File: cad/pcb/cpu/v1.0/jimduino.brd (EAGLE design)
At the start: 38 x 31 mm, 59 parts, among them CN1 SM02B-SRSS-TB, P1 DF12-32-DP, P2 DF12-32-DP, P3 MICROUSB, Q1 FDN360P, Q2 FDN360P, SW1 SWITCH-MOMENTARY-2SMD-REDUNDA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, U1 STM32F415R, U2 MCP1703, U3 MCP73831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

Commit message: Release candidate 0
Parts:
- C7, C8: value 20pF -> 22pF
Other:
- board text removed: "BKUP"
- board text removed: "BOOT0"
- board text removed: "C1"
- board text removed: "C10"
- board text removed: "C11"
- board text removed: "C12"
- board text removed: "C13"
- board text removed: "C14"
- board text removed: "C15"
- board text removed: "C16"
- board text removed: "C17"
- board text removed: "C18"
- board text removed: "C19"
- board text removed: "C2"
- board text removed: "C20"
- board text removed: "C21"
- board text removed: "C3"
- board text removed: "C4"
- board text removed: "C5"
- board text removed: "C6"
- board text removed: "C7"
- board text removed: "C8"
- board text removed: "C9"
- board text removed: "CN1"
- board text removed: "D1"
- board text removed: "D2"
- board text removed: "D3"
- board text removed: "D5"
- board text removed: "F1"
- board text removed: "P1"
- board text removed: "P2"
- board text removed: "POWER"
- board text removed: "Q1"
- board text removed: "Q2"
- board text removed: "R1"
- board text removed: "R10"
- board text removed: "R11"
- board text removed: "R12"
- board text removed: "R2"
- board text removed: "R3"
- board text removed: "R4"
- board text removed: "R5"
- board text removed: "R6"
- board text removed: "R7"
- board text removed: "R8"
- board text removed: "R9"
- board text removed: "RESET"
- board text removed: "SW1"
- board text removed: "U1"
- board text removed: "U2"
- board text removed: "U3"
- board text removed: "U4"
- board text removed: "Y1"

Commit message: Release Candidate 1
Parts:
- C7, C8: value 22pF -> 20pF
- moved C1 0.12 mm to (23.5, 2.75)
- moved C4 0.12 mm to (21.8, 2.75)
- moved C7 0.12 mm to (15.5, 2.75), turned to 90 degrees
- moved C8 0.12 mm to (20.0, 2.75)
- turned R5 to 270 degrees
- turned Y1 to 180 degrees
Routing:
- net PC13: track 35.6 -> 33.1 mm
- net OSC_OUT: track 7.42 -> 5.06 mm
- net GND: track 2.16 -> 0.45 mm, vias 19 -> 17
- net OSC_IN: track 4.88 -> 6.32 mm
- net RESET#: track 74.4 -> 73.3 mm
- net PA2: track 17.0 -> 17.8 mm

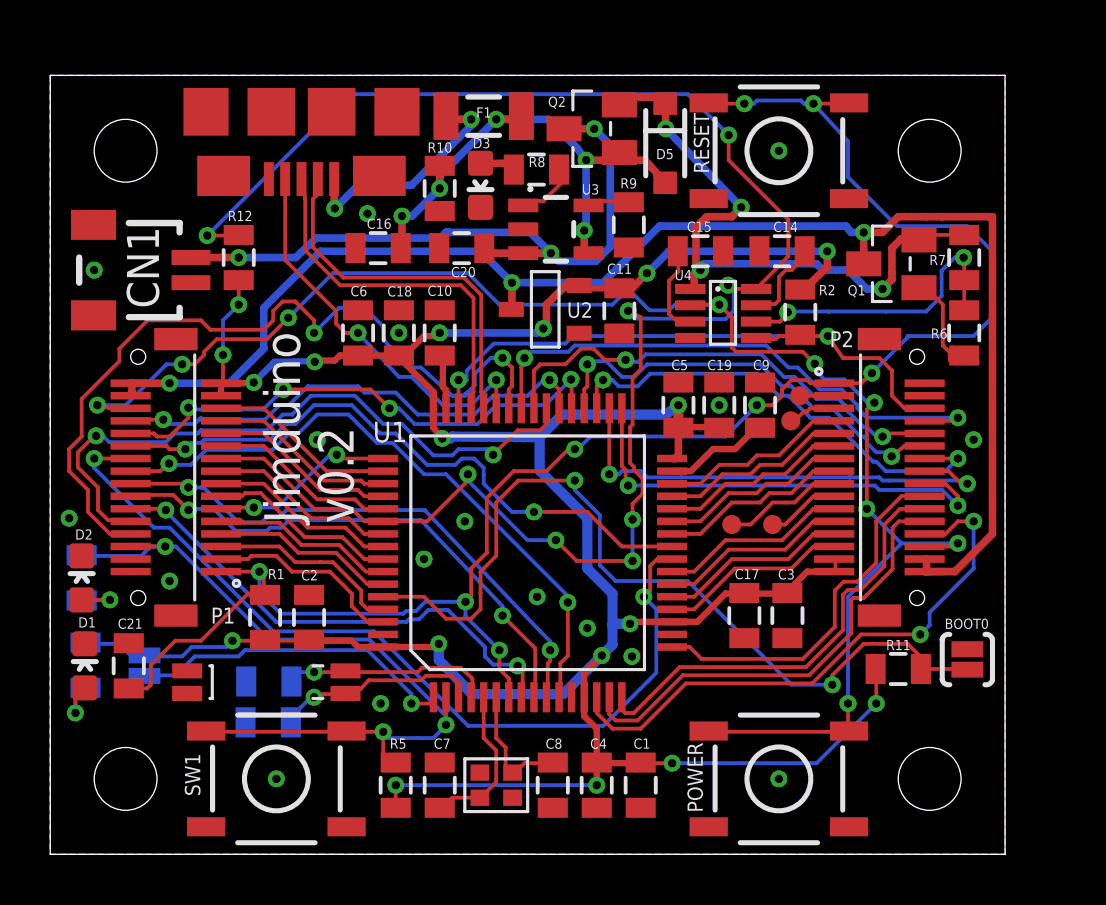
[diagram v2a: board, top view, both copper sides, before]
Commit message: Switch to 0402 capacitors
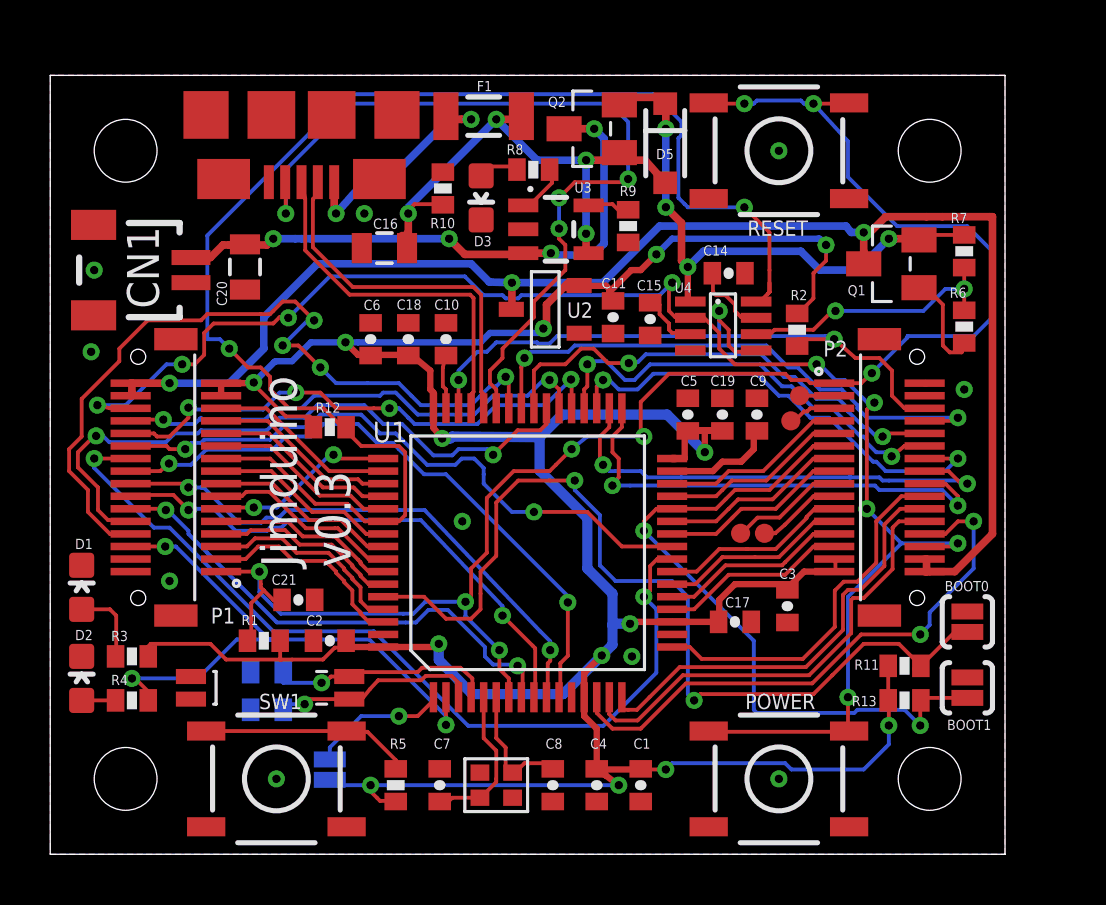
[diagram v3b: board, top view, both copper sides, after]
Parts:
- added BOOT1: JUMPER-PAD-2-NC_BY_PASTE, SparkFun-Passives:PAD-JUMPER-2-NC_BY_PASTE_YES_SILK
- added R13: 10k, SparkFun-Passives:0402-RES
- C1, C10, C11, C12, C13, C14, C15, C17, C18, C19, C2, C21, C3, C4, C5, C6, C7, C8, C9: device SparkFun-Capacitors:0805 -> SparkFun-Capacitors:0402-CAP
- R1, R10, R11, R12, R2, R3, R4, R5, R6, R7, R8, R9: device SparkFun-Passives:0805 -> SparkFun-Passives:0402-RES
- moved C20 8.66 mm to (7.75, 23.4), turned to 270 degrees
- moved BKUP 8.45 mm to (11.1, 3.38), turned to 270 degrees
- moved R12 7.66 mm to (11.1, 17.0), turned to 0 degrees
- moved C21 7.24 mm to (9.88, 10.1), turned to 0 degrees
- moved R4 5.27 mm to (3.25, 6.12), flipped to the top, turned to 0 degrees
- moved D2 4.00 mm to (1.25, 7.00)
- moved C15 3.36 mm to (23.9, 21.3), turned to 270 degrees
- moved D1 3.13 mm to (1.25, 10.6)
- moved C14 2.30 mm to (27.0, 23.1), turned to 0 degrees
- moved R3 1.88 mm to (3.25, 7.88), flipped to the top, turned to 0 degrees
- moved BOOT0 1.50 mm to (36.5, 9.25)
- moved C2 1.24 mm to (11.1, 8.50), turned to 180 degrees
- moved R1 0.93 mm to (8.50, 8.50), turned to 0 degrees
- moved R2 0.71 mm to (29.7, 20.9)
- moved C6 0.56 mm to (12.8, 20.5)
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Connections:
- new net PC14: R5.1, SW1.1, SW1.2
- net GND: now also BOOT1.2
- net PB2: now also BOOT1.1, R13.1
- net PC13: no longer R5.1, SW1.1, SW1.2
- net VCC_3V3: now also R13.2
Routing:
- net PB2: track 7.49 -> 28.0 mm, vias 0 -> 2
- net PA10: track 16.0 -> 33.7 mm, vias 2 -> 4
- net VCC_3V3: track 126.1 -> 142.3 mm, vias 18 -> 14
- net PD2: track 70.4 -> 58.1 mm, vias 8 -> 2
- net PC13: track 33.1 -> 24.5 mm
- net PC14: track 0.00 -> 8.37 mm
- net VCC_BKUP: track 13.6 -> 5.50 mm
- net VBAT: track 28.5 -> 23.7 mm, vias 3 -> 4
- net RESET#: track 73.3 -> 70.0 mm
- net BOOT0: track 34.8 -> 37.8 mm
- net N$3: track 5.33 -> 2.55 mm
- net PA13: track 25.6 -> 28.0 mm, vias 2 -> 3
- net N$8: track 12.8 -> 10.7 mm
- net VCC_SEL: track 26.0 -> 23.9 mm
- net N$4: track 4.50 -> 3.06 mm
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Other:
- board text added: "Jimduino v0.3"
- board text removed: "Jimduino v0.2"

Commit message: Release Candidate 2
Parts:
- BOOT0, BOOT1: value JUMPER-PAD-2-NC_BY_PASTE -> JUMPER-PAD-2-NOYES_SILK; device SparkFun-Passives:PAD-JUMPER-2-NC_BY_PASTE_YES_SILK -> SparkFun-Passives:PAD-JUMPER-2-NO_YES_SILK
- C1, C10, C11, C14, C15, C17, C18, C19, C2, C21, C3, C4, C5, C6, C9: device SparkFun-Capacitors:0402-CAP -> SparkFun-Capacitors:0805
- C12, C13: value 20pF -> 4pF
- C7, C8: value 20pF -> 4pF; device SparkFun-Capacitors:0402-CAP -> SparkFun-Capacitors:0805
- D2: value PC13 -> BOOT1
- R1, R10, R11, R12, R13, R2, R3, R4, R5, R6, R7, R8, R9: device SparkFun-Passives:0402-RES -> SparkFun-Passives:0805
- Y1: value 8Y-16.000MAAV-T -> 16MHz(9pF)
- Y2: value 32.768kHz -> 32.768kHz (9pF)
- moved D1 24.0 mm to (23.2, 1.12), turned to 90 degrees
- moved R3 23.5 mm to (26.7, 6.53)
- moved R4 15.5 mm to (18.0, 1.23)
- moved D2 14.8 mm to (14.9, 1.12), turned to 90 degrees
- moved BKUP 8.98 mm to (3.75, 8.50), turned to 90 degrees
- moved C20 8.80 mm to (16.4, 25.1), turned to 180 degrees
- moved R12 8.56 mm to (7.50, 24.8), turned to 90 degrees
- moved C21 6.94 mm to (3.12, 8.50), turned to 90 degrees
- moved C15 4.21 mm to (25.9, 25.0), turned to 0 degrees
- moved C14 2.83 mm to (29.1, 25.0), turned to 180 degrees
- moved C2 2.09 mm to (10.3, 10.4), turned to 90 degrees
- moved R1 1.93 mm to (8.55, 10.4), turned to 270 degrees
- moved C13 1.85 mm to (7.05, 6.28), flipped to the top, turned to 180 degrees
- moved R2 1.70 mm to (29.9, 22.6)
- moved C12 1.52 mm to (10.1, 6.28), flipped to the top
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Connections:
- removed net PC14: R5.1, SW1.1, SW1.2
- net GND: now also R11.2, R13.2; no longer BOOT0.2, BOOT1.2
- net PB2: now also R4.2
- net PC13: now also R5.1, SW1.1, SW1.2; no longer R4.2
- net VCC_3V3: now also BOOT0.2, BOOT1.2; no longer R11.2, R13.2
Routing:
- net PB2: track 28.0 -> 47.0 mm, vias 2 -> 4
- net PA10: track 33.7 -> 16.0 mm, vias 4 -> 2
- net PD2: track 58.1 -> 70.9 mm, vias 2 -> 8
- net PC14: track 8.37 -> 0.00 mm
- net VCC_BKUP: track 5.50 -> 13.6 mm
- net VCC_3V3: track 142.3 -> 135.2 mm, vias 14 -> 18
- net PC13: track 24.5 -> 31.2 mm
- net VBAT: track 23.7 -> 28.5 mm, vias 4 -> 3
- net PWR_ON: track 62.7 -> 67.0 mm
- net N$5: track 3.13 -> 7.34 mm, vias 0 -> 1
- net RESET#: track 70.0 -> 73.3 mm
- net N$3: track 2.55 -> 5.33 mm
- net BOOT0: track 37.8 -> 35.2 mm
- net PA13: track 28.0 -> 25.6 mm, vias 3 -> 2
- net N$8: track 10.7 -> 12.8 mm
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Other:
- board size 38 x 31 mm -> 38 x 32 mm
- board text added: "MatchBox v1.0"
- board text removed: "Jimduino v0.3"

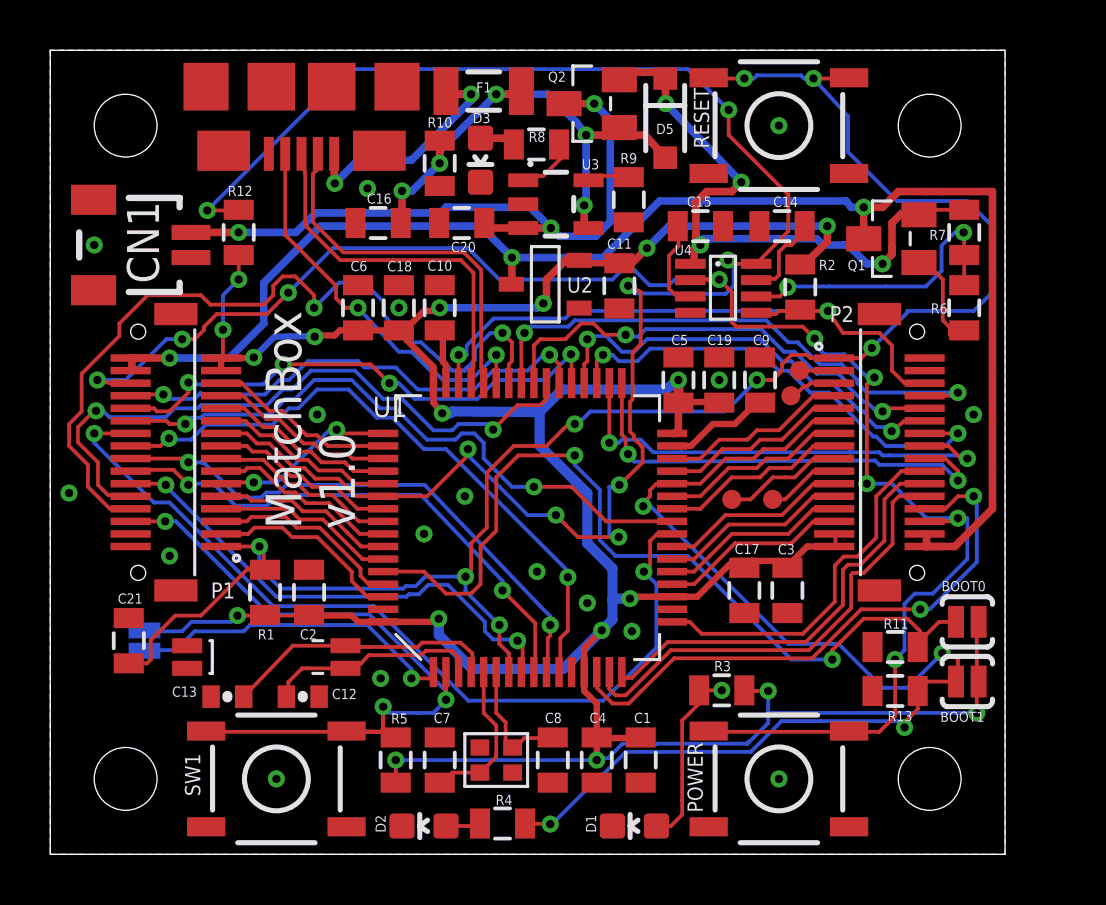
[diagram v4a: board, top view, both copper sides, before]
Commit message: New USB connector
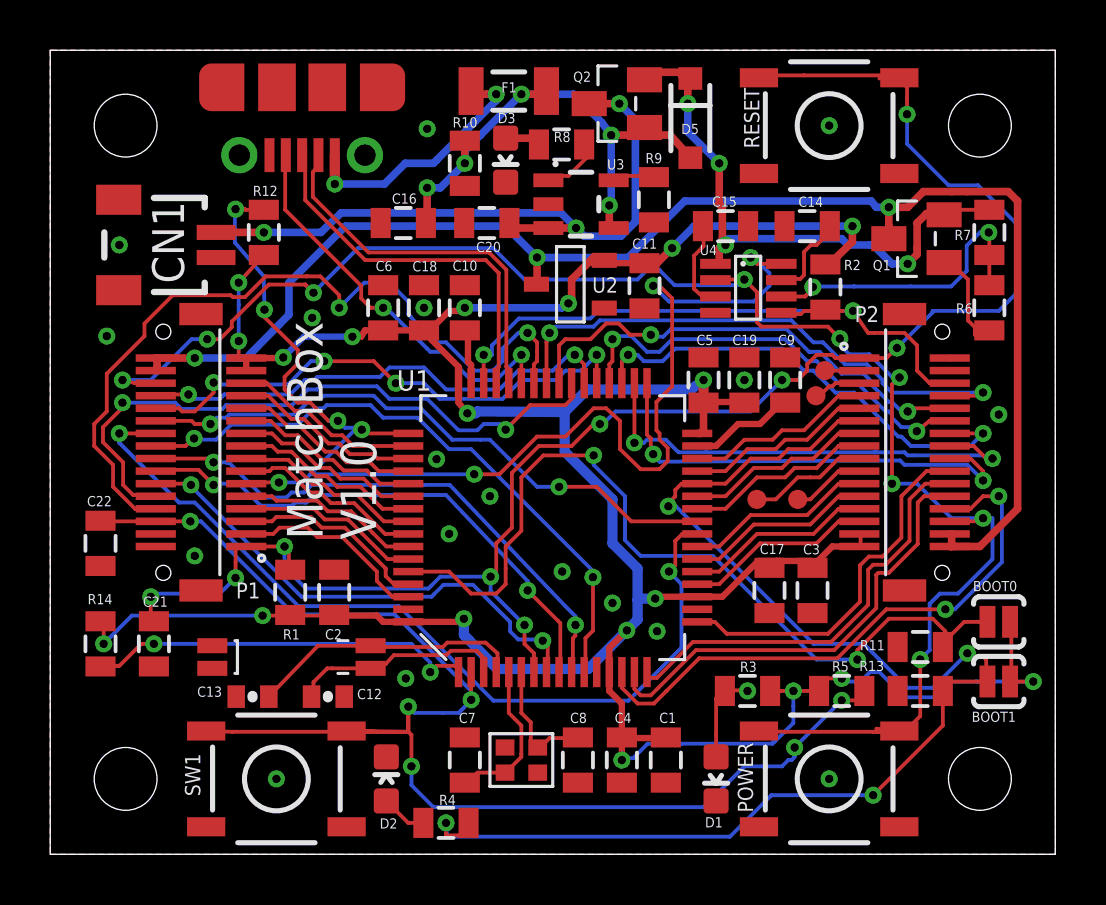
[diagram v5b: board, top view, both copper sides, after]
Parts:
- removed BKUP: JUMPER-PAD-2-NC_BY_PASTE, SparkFun-Passives:PAD-JUMPER-2-NC_BY_PASTE_YES_SILK
- removed P3: MICROUSB, jimduino:MICROUSB
- added C22: 0.1uF, SparkFun-Capacitors:0805
- added R14: 0k, SparkFun-Passives:0805
- added U$1: USB-CON-5PIN-105017-0001, GeekAmmo:USB-MICRO-MOLEX-105017-0001
- D2: value BOOT1 -> PB2
- moved R5 18.0 mm to (31.5, 6.50), turned to 180 degrees
- moved D1 3.75 mm to (26.5, 3.00), turned to 180 degrees
- moved D2 2.40 mm to (13.4, 3.00), turned to 0 degrees
- moved R4 2.25 mm to (15.8, 1.25)
- moved POWER 2.00 mm to (31.0, 3.00)
- moved RESET 2.00 mm to (31.0, 29.0)
- moved BOOT0 1.25 mm to (37.8, 9.25)
- moved BOOT1 1.25 mm to (37.8, 6.88)
- moved R3 1.03 mm to (27.8, 6.50)
- moved C21 1.01 mm to (4.12, 8.38), turned to 270 degrees
- moved C13 1.00 mm to (8.05, 6.28)
- moved C1 1.00 mm to (24.5, 3.75)
- moved C10 1.00 mm to (16.5, 21.8)
- moved C11 1.00 mm to (23.6, 22.6)
- moved C12 1.00 mm to (11.1, 6.28)
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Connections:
- net GND: now also C22.2, U$1.5; no longer P3.10, P3.11, P3.5, P3.6, P3.7, P3.8, P3.9
- net PA10: now also U$1.4; no longer P3.4
- net PA11: now also U$1.2; no longer P3.2
- net PA12: now also U$1.3; no longer P3.3
- net PA14: now also R12.2, U4.8
- net PC13: now also C22.1
- net PD2: no longer R12.2, U4.8
- net VCC_3V3: now also R14.1; no longer BKUP.2
- net VCC_BKUP: now also R14.2; no longer BKUP.1
- net VCC_USB: now also U$1.1; no longer P3.1
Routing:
- net PD2: track 70.9 -> 7.49 mm, vias 8 -> 0
- net PA14: track 7.71 -> 54.1 mm, vias 2 -> 8
- net PC13: track 31.2 -> 60.8 mm, vias 3 -> 6
- net PB2: track 47.0 -> 54.0 mm
- net N$5: track 7.34 -> 3.69 mm
- net VCC_3V3: track 135.2 -> 132.1 mm, vias 18 -> 19
- net PWR_ON: track 67.0 -> 69.4 mm
- net VCC_BKUP: track 13.6 -> 15.8 mm, vias 1 -> 2
- net RESET#: track 73.3 -> 71.8 mm, vias 8 -> 9
- net VCC_SEL: track 26.0 -> 24.8 mm
- net PC5: track 25.2 -> 24.1 mm
- net VCC_USB: track 9.40 -> 10.4 mm
- net PA12: track 14.8 -> 15.7 mm
- net VBAT: track 28.5 -> 27.8 mm
- net PC3: track 25.6 -> 25.1 mm
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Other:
- board size 38 x 32 mm -> 40 x 32 mm
- board text added: "MatchBox V1.0"
- board text removed: "MatchBox v1.0"

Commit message: unknown changes
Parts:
- C12, C13: value 4pF -> 8pF
- U$1: value USB-CON-5PIN-105017-0001 -> MICROUSB; device GeekAmmo:USB-MICRO-MOLEX-105017-0001 -> jimduino:MICROUSB
- moved U$1 3.72 mm to (10.0, 30.6)
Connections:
- net GND: now also U$1.10, U$1.11, U$1.6, U$1.7, U$1.8, U$1.9
